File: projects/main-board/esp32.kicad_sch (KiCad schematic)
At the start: 21 parts, among them J4 USB4105-GF-A, J5 TC2030, U9 ESP32-C6FH4, Y1 ABM10W-40.0000MHZ-8-B1U-T3

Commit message: Replace placeholder resistors
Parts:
- removed R51, R53: 5.1K, symbol Device:R_Small_US
- removed R52: 10K, symbol Device:R_Small_US
- removed R54: TBD, symbol Device:R_Small_US
- added R47: 10K, Resistor_SMD:R_0402_1005Metric, symbol symbol-library-resistors:RC0402JR-0710KL
- added R48, R49: 5.1K, Resistor_SMD:R_0402_1005Metric, symbol symbol-library-resistors:RC0402FR-075K1L
- added R50: 0R, Resistor_SMD:R_0402_1005Metric, symbol symbol-library-resistors:RC0402FR-070RL
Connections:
- net ESP32_EN: now also R47.1
- net GND: now also R47.2, R48.2, R49.2
- net at J4.B5 (CC2): now also R49.1
- net at J4.A5 (CC1): now also R48.1
- net at U9.31 (XTAL_P): now also R50.1
- net at C83.1, Y1.1: now also R50.2
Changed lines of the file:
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@@
+	)
+	(symbol
+		(lib_id "symbol-library-resistors:RC0402FR-075K1L")
+		(at 46.99 156.21 0)
+		(unit 1)
+		(exclude_from_sim no)
+		(in_bom yes)
+		(on_board yes)
+		(dnp no)
+		(fields_autoplaced yes)
+		(property "Reference" "R48"
+			(at 49.53 154.9399 0)
+			(effects
+				(font
+					(size 1.27 1.27)
+				)
+				(justify left)
+			)
+		)
+		(property "Value" "5.1K"
+			(at 49.53 157.4799 0)
+			(effects
+				(font
+					(size 1.27 1.27)
+				)
+				(justify left)
+			)
+		)
+		(property "Footprint" "Resistor_SMD:R_0402_1005Metric"
+			(at 46.99 156.21 0)
+			(effects
+				(font
+					(size 1.27 1.27)
+				)
+				(hide yes)
+			)
+		)
+		(property "Datasheet" "~"
+			(at 46.99 156.21 0)
+			(effects
+				(font
+					(size 1.27 1.27)
+				)
+				(hide yes)
+			)
+		)
+		(property "Description" "Resistor, small US symbol"
+			(at 46.99 156.21 0)
+			(effects
+				(font
+					(size 1.27 1.27)
+				)
+				(hide yes)
+			)
+		)
+		(pin "2"
+		)
+		(pin "1"
+		)
+		(instances
+			(project "main-board"
+				(path "/c621b5fd-2ef7-4a67-960d-0ffc72b1245a/9604ec8b-dd8b-4641-a93a-60fcfb624c0c"
+					(reference "R48")
+					(unit 1)
+				)
+			)
+		)
 	)
 	(symbol
@@
 	)
 	(symbol
-		(lib_id "Device:R_Small_US")
+		(lib_id "symbol-library-resistors:RC0402FR-075K1L")
 		(at 55.88 156.21 0)
 		(unit 1)
@@
 		(dnp no)
 		(fields_autoplaced yes)
-		(property "Reference" "R53"
+		(property "Reference" "R49"
 			(at 58.42 154.9399 0)
 			(effects
@@
 			)
 		)
-		(property "Footprint" ""
+		(property "Footprint" "Resistor_SMD:R_0402_1005Metric"
 			(at 55.88 156.21 0)
 			(effects
@@
 			)
 		)
-		(pin "1"
-		)
 		(pin "2"
 		)
-		(instances
-			(project "main-board"
-				(path "/c621b5fd-2ef7-4a67-960d-0ffc72b1245a/9604ec8b-dd8b-4641-a93a-60fcfb624c0c"
-					(reference "R53")
-					(unit 1)
-				)
-			)
-		)
-	)
-	(symbol
-		(lib_id "Device:R_Small_US")
-		(at 46.99 156.21 0)
-		(unit 1)
-		(exclude_from_sim no)
-		(in_bom yes)
-		(on_board yes)
-		(dnp no)
-		(fields_autoplaced yes)
-		(property "Reference" "R51"
-			(at 49.53 154.9399 0)
-			(effects
-				(font
-					(size 1.27 1.27)
-				)
-				(justify left)
-			)
-		)
-		(property "Value" "5.1K"
-			(at 49.53 157.4799 0)
-			(effects
-				(font
-					(size 1.27 1.27)
-				)
-				(justify left)
-			)
-		)
-		(property "Footprint" ""
-			(at 46.99 156.21 0)
-			(effects
-				(font
-					(size 1.27 1.27)
-				)
-				(hide yes)
-			)
-		)
-		(property "Datasheet" "~"
-			(at 46.99 156.21 0)
-			(effects
-				(font
-					(size 1.27 1.27)
-				)
-				(hide yes)
-			)
-		)
-		(property "Description" "Resistor, small US symbol"
-			(at 46.99 156.21 0)
-			(effects
-				(font
-					(size 1.27 1.27)
-				)
-				(hide yes)
-			)
-		)
-		(pin "1"
-		)
-		(pin "2"
-		)
-		(instances
-			(project "main-board"
-				(path "/c621b5fd-2ef7-4a67-960d-0ffc72b1245a/9604ec8b-dd8b-4641-a93a-60fcfb624c0c"
-					(reference "R51")
+		(pin "1"
+		)
+		(instances
+			(project "main-board"
+				(path "/c621b5fd-2ef7-4a67-960d-0ffc72b1245a/9604ec8b-dd8b-4641-a93a-60fcfb624c0c"
+					(reference "R49")
 					(unit 1)
 				)
@@
 	)
 	(symbol
-		(lib_id "Device:R_Small_US")
-		(at 193.04 85.09 90)
-		(unit 1)
-		(exclude_from_sim no)
-		(in_bom yes)
-		(on_board yes)
-		(dnp no)
-		(property "Reference" "R54"
-			(at 189.484 83.058 90)
-			(effects
-				(font
-					(size 1.27 1.27)
-				)
-			)
-		)
-		(property "Value" "TBD"
-			(at 196.596 83.058 90)
-			(effects
-				(font
-					(size 1.27 1.27)
-				)
-			)
-		)
-		(property "Footprint" ""
-			(at 193.04 85.09 0)
-			(effects
-				(font
-					(size 1.27 1.27)
-				)
-				(hide yes)
-			)
-		)
-		(property "Datasheet" "~"
-			(at 193.04 85.09 0)
-			(effects
-				(font
-					(size 1.27 1.27)
-				)
-				(hide yes)
-			)
-		)
-		(property "Description" "Resistor, small US symbol"
-			(at 193.04 85.09 0)
-			(effects
-				(font
-					(size 1.27 1.27)
-				)
-				(hide yes)
-			)
-		)
-		(pin "1"
-		)
-		(pin "2"
-		)
-		(instances
-			(project ""
-				(path "/c621b5fd-2ef7-4a67-960d-0ffc72b1245a/9604ec8b-dd8b-4641-a93a-60fcfb624c0c"
-					(reference "R54")
-					(unit 1)
-				)
-			)
-		)
-	)
-	(symbol
 		(lib_id "Connector:TC2030")
 		(at 140.97 144.78 0)
@@
 				(path "/c621b5fd-2ef7-4a67-960d-0ffc72b1245a/9604ec8b-dd8b-4641-a93a-60fcfb624c0c"
 					(reference "J5")
+					(unit 1)
+				)
+			)
+		)
+	)
+	(symbol
+		(lib_id "symbol-library-resistors:RC0402JR-0710KL")
+		(at 54.61 50.8 0)
+		(unit 1)
+		(exclude_from_sim no)
+		(in_bom yes)
+		(on_board yes)
+		(dnp no)
+		(fields_autoplaced yes)
+		(property "Reference" "R47"
+			(at 57.15 49.5299 0)
+			(effects
+				(font
+					(size 1.27 1.27)
+				)
+				(justify left)
+			)
+		)
+		(property "Value" "10K"
+			(at 57.15 52.0699 0)
+			(effects
+				(font
+					(size 1.27 1.27)
+				)
+				(justify left)
+			)
+		)
+		(property "Footprint" "Resistor_SMD:R_0402_1005Metric"
+			(at 54.61 50.8 0)
+			(effects
+				(font
+					(size 1.27 1.27)
+				)
+				(hide yes)
+			)
+		)
+		(property "Datasheet" "~"
+			(at 54.61 50.8 0)
+			(effects
+				(font
+					(size 1.27 1.27)
+				)
+				(hide yes)
+			)
+		)
+		(property "Description" "Resistor, small US symbol"
+			(at 54.61 50.8 0)
+			(effects
+				(font
+					(size 1.27 1.27)
+				)
+				(hide yes)
+			)
+		)
+		(pin "1"
+		)
+		(pin "2"
+		)
+		(instances
+			(project "main-board"
+				(path "/c621b5fd-2ef7-4a67-960d-0ffc72b1245a/9604ec8b-dd8b-4641-a93a-60fcfb624c0c"
+					(reference "R47")
 					(unit 1)
 				)
@@
 	)
 	(symbol
-		(lib_id "Device:R_Small_US")
-		(at 54.61 50.8 0)
-		(unit 1)
-		(exclude_from_sim no)
-		(in_bom yes)
-		(on_board yes)
-		(dnp no)
-		(fields_autoplaced yes)
-		(property "Reference" "R52"
-			(at 57.15 49.5299 0)
-			(effects
-				(font
-					(size 1.27 1.27)
-				)
-				(justify left)
-			)
-		)
-		(property "Value" "10K"
-			(at 57.15 52.0699 0)
-			(effects
-				(font
-					(size 1.27 1.27)
-				)
-				(justify left)
-			)
-		)
-		(property "Footprint" ""
-			(at 54.61 50.8 0)
-			(effects
-				(font
-					(size 1.27 1.27)
-				)
-				(hide yes)
-			)
-		)
-		(property "Datasheet" "~"
-			(at 54.61 50.8 0)
-			(effects
-				(font
-					(size 1.27 1.27)
-				)
-				(hide yes)
-			)
-		)
-		(property "Description" "Resistor, small US symbol"
-			(at 54.61 50.8 0)
-			(effects
-				(font
-					(size 1.27 1.27)
-				)
-				(hide yes)
-			)
-		)
-		(pin "1"
-		)
-		(pin "2"
-		)
-		(instances
-			(project "main-board"
-				(path "/c621b5fd-2ef7-4a67-960d-0ffc72b1245a/9604ec8b-dd8b-4641-a93a-60fcfb624c0c"
-					(reference "R52")
-					(unit 1)
-				)
-			)
-		)
-	)
-	(symbol
 		(lib_id "power:GND")
 		(at 105.41 184.15 0)
@@
 					(unit 1)
 				)
+			)
+		)
+	)
+	(symbol
+		(lib_id "symbol-library-resistors:RC0402FR-070RL")
+		(at 193.04 85.09 90)
+		(unit 1)
+		(exclude_from_sim no)
+		(in_bom yes)
+		(on_board yes)
+		(dnp no)
+		(property "Reference" "R50"
+			(at 189.992 82.804 90)
+			(effects
+				(font
+					(size 1.27 1.27)
+				)
+			)
+		)
+		(property "Value" "0R"
+			(at 195.072 82.55 90)
+			(effects
+				(font
+					(size 1.27 1.27)
+				)
+			)
+		)
+		(property "Footprint" "Resistor_SMD:R_0402_1005Metric"
+			(at 193.04 85.09 0)
+			(effects
+				(font
+					(size 1.27 1.27)
+				)
+				(hide yes)
+			)
+		)
+		(property "Datasheet" "~"
+			(at 193.04 85.09 0)
+			(effects
+				(font
+					(size 1.27 1.27)
+				)
+				(hide yes)
+			)
+		)
+		(property "Description" "Resistor, small US symbol"
+			(at 193.04 85.09 0)
+			(effects
+				(font
+					(size 1.27 1.27)
+				)
+				(hide yes)
+			)
+		)
+		(pin "1"
+		)
+		(pin "2"
+		)
+		(instances
+			(project ""
+				(path "/c621b5fd-2ef7-4a67-960d-0ffc72b1245a/9604ec8b-dd8b-4641-a93a-60fcfb624c0c"
+					(reference "R50")
+					(unit 1)
+				)

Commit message: Add footprints
- Inductors
- Switches
- Buttons
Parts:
- renumbered L4 to L5, R48 to R51, R47 to R52, R49 to R53, R50 to R54
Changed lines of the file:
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@@
 		(dnp no)
 		(fields_autoplaced yes)
-		(property "Reference" "R48"
+		(property "Reference" "R51"
 			(at 49.53 154.9399 0)
 			(effects
@@
 			(project "main-board"
 				(path "/c621b5fd-2ef7-4a67-960d-0ffc72b1245a/9604ec8b-dd8b-4641-a93a-60fcfb624c0c"
-					(reference "R48")
+					(reference "R51")
 					(unit 1)
 				)
@@
 		(dnp no)
 		(fields_autoplaced yes)
-		(property "Reference" "R49"
+		(property "Reference" "R53"
 			(at 58.42 154.9399 0)
 			(effects
@@
 			(project "main-board"
 				(path "/c621b5fd-2ef7-4a67-960d-0ffc72b1245a/9604ec8b-dd8b-4641-a93a-60fcfb624c0c"
-					(reference "R49")
+					(reference "R53")
 					(unit 1)
 				)
@@
 		(on_board yes)
 		(dnp no)
-		(property "Reference" "L4"
+		(property "Reference" "L5"
 			(at 210.82 21.844 90)
 			(effects
@@
 			(project ""
 				(path "/c621b5fd-2ef7-4a67-960d-0ffc72b1245a/9604ec8b-dd8b-4641-a93a-60fcfb624c0c"
-					(reference "L4")
+					(reference "L5")
 					(unit 1)
 				)
@@
 		(dnp no)
 		(fields_autoplaced yes)
-		(property "Reference" "R47"
+		(property "Reference" "R52"
 			(at 57.15 49.5299 0)
 			(effects
@@
 			(project "main-board"
 				(path "/c621b5fd-2ef7-4a67-960d-0ffc72b1245a/9604ec8b-dd8b-4641-a93a-60fcfb624c0c"
-					(reference "R47")
+					(reference "R52")
 					(unit 1)
 				)
@@
 		(dnp no)
 		(fields_autoplaced yes)
-		(property "Reference" "#PWR0116"
+		(property "Reference" "#PWR0117"
 			(at 46.99 167.64 0)
 			(effects
@@
 			(project "main-board"
 				(path "/c621b5fd-2ef7-4a67-960d-0ffc72b1245a/9604ec8b-dd8b-4641-a93a-60fcfb624c0c"
-					(reference "#PWR0116")
+					(reference "#PWR0117")
 					(unit 1)
 				)
@@
 		(dnp no)
 		(fields_autoplaced yes)
-		(property "Reference" "#PWR0120"
+		(property "Reference" "#PWR0121"
 			(at 186.69 119.38 0)
 			(effects
@@
 			(project ""
 				(path "/c621b5fd-2ef7-4a67-960d-0ffc72b1245a/9604ec8b-dd8b-4641-a93a-60fcfb624c0c"
-					(reference "#PWR0120")
+					(reference "#PWR0121")
 					(unit 1)
 				)
@@
 		(on_board yes)
 		(dnp no)
-		(property "Reference" "#PWR0119"
+		(property "Reference" "#PWR0120"
 			(at 134.62 154.94 0)
 			(effects
@@
 			(project "main-board"
 				(path "/c621b5fd-2ef7-4a67-960d-0ffc72b1245a/9604ec8b-dd8b-4641-a93a-60fcfb624c0c"
-					(reference "#PWR0119")
+					(reference "#PWR0120")
 					(unit 1)
 				)
@@
 		(on_board yes)
 		(dnp no)
-		(property "Reference" "#PWR0118"
+		(property "Reference" "#PWR0119"
 			(at 105.41 190.5 0)
 			(effects
@@
 			(project "main-board"
 				(path "/c621b5fd-2ef7-4a67-960d-0ffc72b1245a/9604ec8b-dd8b-4641-a93a-60fcfb624c0c"
-					(reference "#PWR0118")
+					(reference "#PWR0119")
 					(unit 1)
 				)
@@
 		(dnp no)
 		(fields_autoplaced yes)
-		(property "Reference" "#PWR0121"
+		(property "Reference" "#PWR0122"
 			(at 220.98 100.33 0)
 			(effects
@@
 			(project "main-board"
 				(path "/c621b5fd-2ef7-4a67-960d-0ffc72b1245a/9604ec8b-dd8b-4641-a93a-60fcfb624c0c"
-					(reference "#PWR0121")
+					(reference "#PWR0122")
 					(unit 1)
 				)
@@
 		(dnp no)
 		(fields_autoplaced yes)
-		(property "Reference" "#PWR0115"
+		(property "Reference" "#PWR0116"
 			(at 29.21 55.88 0)
 			(effects
@@
 			(project "main-board"
 				(path "/c621b5fd-2ef7-4a67-960d-0ffc72b1245a/9604ec8b-dd8b-4641-a93a-60fcfb624c0c"
-					(reference "#PWR0115")
+					(reference "#PWR0116")
 					(unit 1)
 				)
@@
 		(on_board yes)
 		(dnp no)
-		(property "Reference" "R50"
+		(property "Reference" "R54"
 			(at 189.992 82.804 90)
 			(effects
@@
 			(project ""
 				(path "/c621b5fd-2ef7-4a67-960d-0ffc72b1245a/9604ec8b-dd8b-4641-a93a-60fcfb624c0c"
-					(reference "R50")
+					(reference "R54")
 					(unit 1)
 				)
@@
 		(dnp no)
 		(fields_autoplaced yes)
-		(property "Reference" "#PWR0117"
+		(property "Reference" "#PWR0118"
 			(at 54.61 60.96 0)
 			(effects
@@
 			(project "main-board"
 				(path "/c621b5fd-2ef7-4a67-960d-0ffc72b1245a/9604ec8b-dd8b-4641-a93a-60fcfb624c0c"
-					(reference "#PWR0117")
+					(reference "#PWR0118")
 					(unit 1)
 				)
@@
 		(dnp no)
 		(fields_autoplaced yes)
-		(property "Reference" "#PWR0114"
+		(property "Reference" "#PWR0115"
 			(at 29.21 26.67 0)
 			(effects
@@
 			(project "main-board"
 				(path "/c621b5fd-2ef7-4a67-960d-0ffc72b1245a/9604ec8b-dd8b-4641-a93a-60fcfb624c0c"
-					(reference "#PWR0114")
+					(reference "#PWR0115")
 					(unit 1)
 				)
@@
 		(dnp no)
 		(fields_autoplaced yes)
-		(property "Reference" "#PWR0122"
+		(property "Reference" "#PWR0123"
 			(at 223.52 39.37 0)
 			(effects
@@
 			(project "main-board"
 				(path "/c621b5fd-2ef7-4a67-960d-0ffc72b1245a/9604ec8b-dd8b-4641-a93a-60fcfb624c0c"
-					(reference "#PWR0122")
-					(unit 1)
-				)
+					(reference "#PWR0123")
+					(unit 1)
+				)

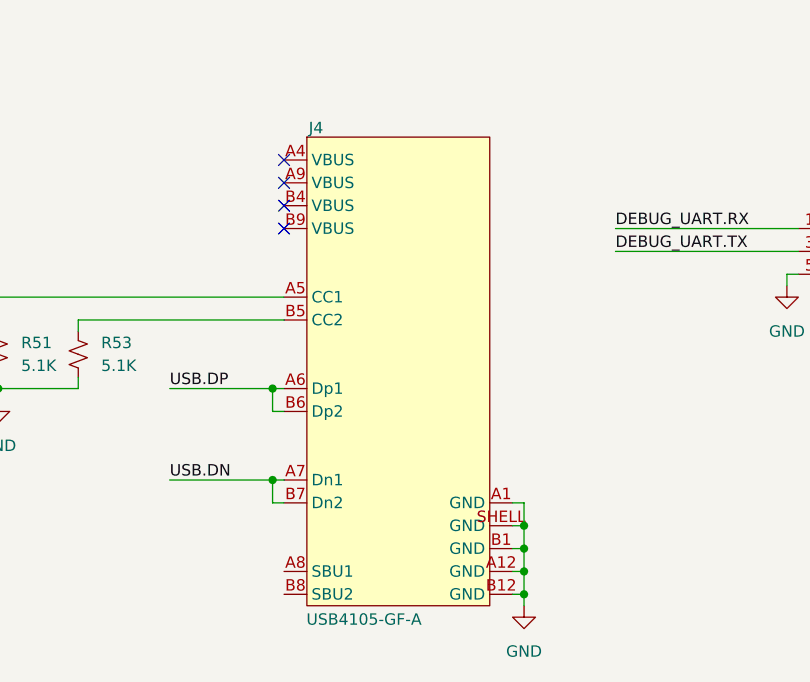
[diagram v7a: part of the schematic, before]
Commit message: Fix footprint DRC errors.
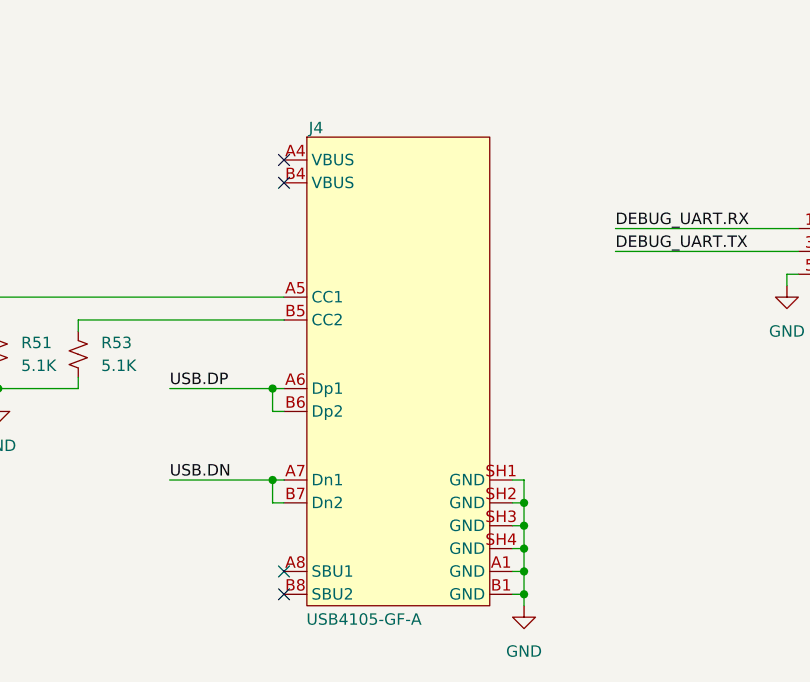
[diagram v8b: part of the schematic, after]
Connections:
- net GND: now also J4.SH1 (GND), J4.SH2 (GND), J4.SH3 (GND), J4.SH4 (GND); no longer J4.A12 (GND), J4.B12 (GND), J4.SHELL (GND)
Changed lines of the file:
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@@
+	)
+	(junction
+		(at 105.41 172.72)
+		(diameter 0)
+		(color 0 0 0 0)
 	)
 	(junction
@@
 	)
 	(no_connect
-		(at 78.74 139.7)
-	)
-	(no_connect
 		(at 185.42 63.5)
-	)
-	(no_connect
-		(at 78.74 142.24)
 	)
 	(no_connect
 		(at 185.42 60.96)
+	)
+	(no_connect
+		(at 78.74 180.34)
+	)
+	(no_connect
+		(at 78.74 182.88)
 	)
 	(no_connect
@@
 	(wire
 		(pts
+			(xy 105.41 170.18) (xy 105.41 172.72)
+		)
+		(stroke
+			(width 0)
+			(type default)
+		)
+	)
+	(wire
+		(pts
 			(xy 46.99 149.86) (xy 46.99 153.67)
 		)
@@
 		(pts
 			(xy 128.27 29.21) (xy 129.54 29.21)
+		)
+		(stroke
+			(width 0)
+			(type default)
+		)
+	)
+	(wire
+		(pts
+			(xy 104.14 170.18) (xy 105.41 170.18)
 		)
 		(stroke
@@
 	)
 	(symbol
-		(lib_name "USB4105-GF-A_1")
 		(lib_id "symbol-library:USB4105-GF-A")
 		(at 81.28 132.08 0)
@@
 		(pin "A1"
 		)
-		(pin "SHELL"
+		(pin "SH1"
 		)
 		(pin "B1"
 		)
-		(pin "A12"
-		)
-		(pin "B12"
-		)
-		(pin "B9"
-		)
 		(pin "A4"
 		)
-		(pin "A9"
-		)
 		(pin "B4"
 		)
+		(pin "SH2"
+		)
+		(pin "SH3"
+		)
+		(pin "SH4"
+		)
 		(instances
